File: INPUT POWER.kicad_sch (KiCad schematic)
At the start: 1 part, among them J1 TYPE-C-31-M12_13

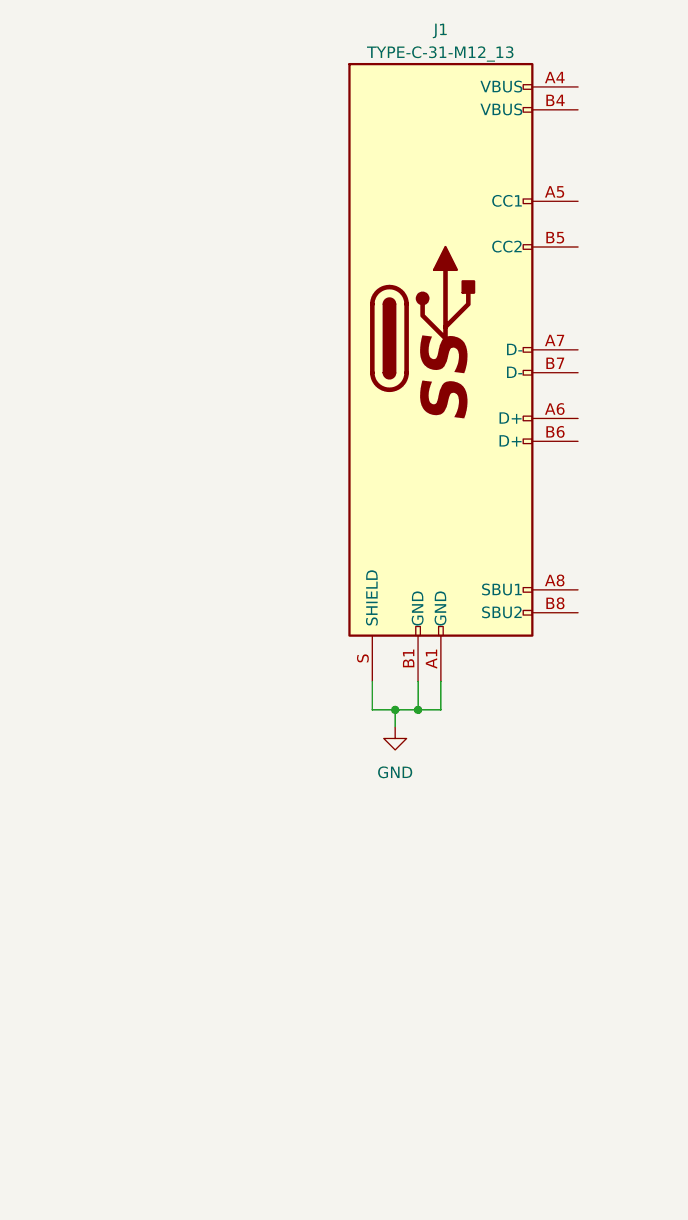
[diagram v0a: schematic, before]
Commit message: completed USB-C wiring and added flash
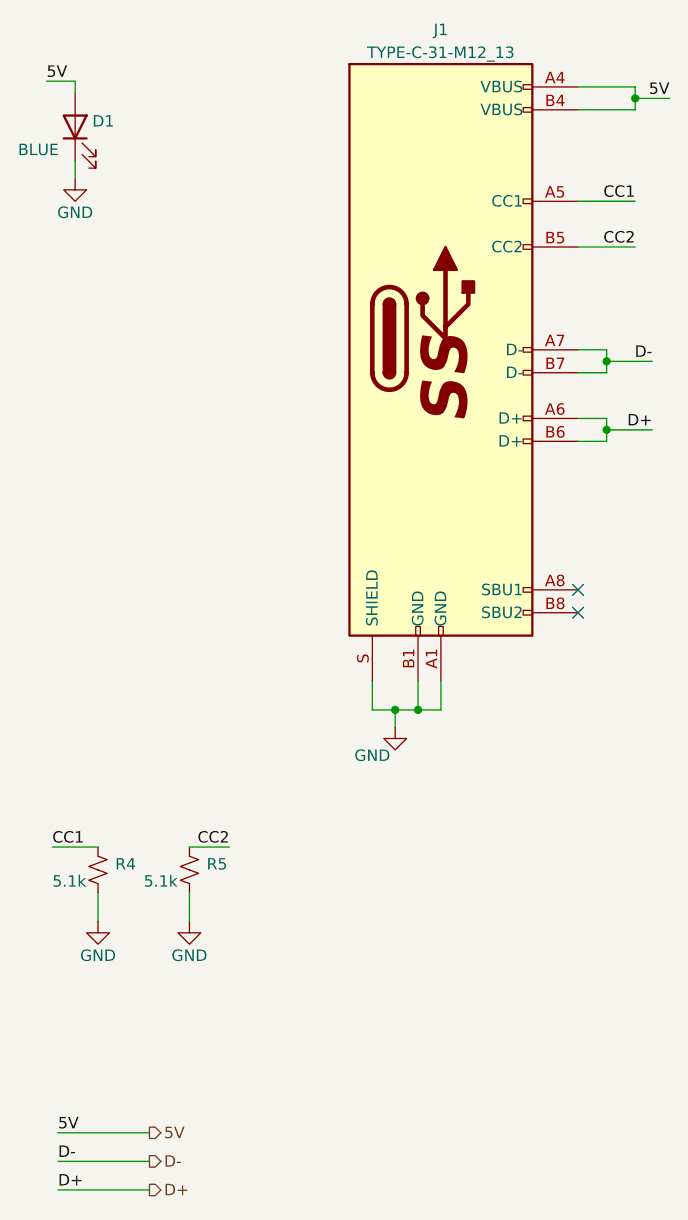
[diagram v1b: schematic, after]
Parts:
- added D1: BLUE, symbol ESP32-S3_DB:LED
- added R4, R5: 5.1k, symbol ESP32-S3_DB:R_Small_US
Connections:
- net GND: now also D1.1 (K), R4.2, R5.2
- net 5V: now reaches J1.A4 (VBUS)
- net 5V: now also J1.B4 (VBUS), D1.2 (A)
- net CC1: now reaches J1.A5 (CC1)
- net CC1: now also R4.1
- net D+: now reaches J1.A6 (D+)
- net D+: now also J1.B6 (D+)
- net D-: now reaches J1.A7 (D-)
- net D-: now also J1.B7 (D-)
- net CC2: now reaches J1.B5 (CC2)
- net CC2: now also R5.1
- no-connect marks 0 -> 2

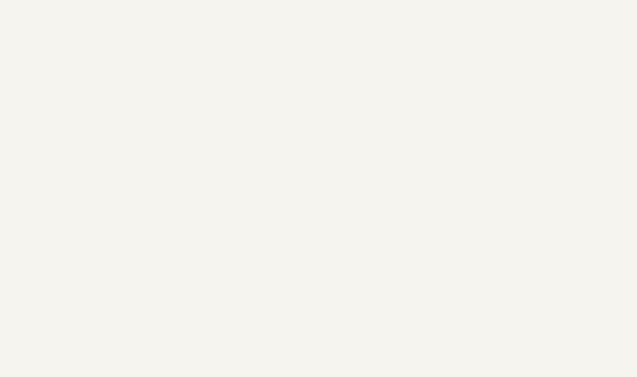
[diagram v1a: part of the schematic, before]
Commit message: Added USB-To-UART Converter
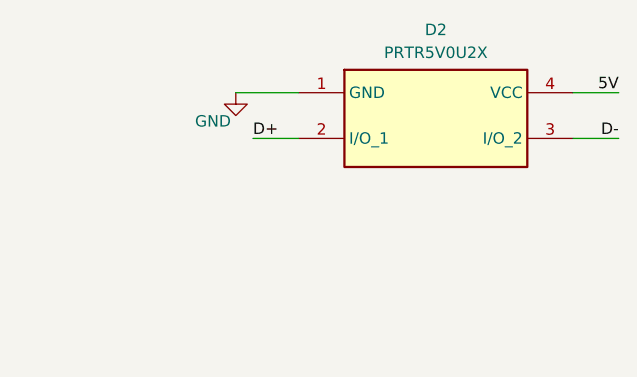
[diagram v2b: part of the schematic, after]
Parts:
- added D2: PRTR5V0U2X, PRTR5V0U2X, symbol ESP32-S3_DB:PRTR5V0U2X
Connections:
- net 5V: now also D2.4 (VCC)
- net D+: now also D2.2 (I/O_1)
- net D-: now also D2.3 (I/O_2)
- net GND: now also D2.1 (GND)
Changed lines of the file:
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@@
+    (stroke (width 0) (type default))
+  )
+  (wire (pts (xy 181.61 36.195) (xy 186.69 36.195))
     (stroke (width 0) (type default))
   )
@@
     (stroke (width 0) (type default))
   )
+  (wire (pts (xy 186.69 31.115) (xy 181.61 31.115))
+    (stroke (width 0) (type default))
+  )
   (wire (pts (xy 66.675 132.08) (xy 66.675 135.255))
     (stroke (width 0) (type default))
@@
     (stroke (width 0) (type default))
   )
+  (wire (pts (xy 146.05 36.195) (xy 151.13 36.195))
+    (stroke (width 0) (type default))
+  )
   (wire (pts (xy 85.09 105.41) (xy 81.915 105.41))
     (stroke (width 0) (type default))
@@
     (stroke (width 0) (type default))
   )
+  (wire (pts (xy 144.145 31.115) (xy 151.13 31.115))
+    (stroke (width 0) (type default))
+  )
   (wire (pts (xy 59.055 135.255) (xy 61.595 135.255))
     (stroke (width 0) (type default))
@@
     (stroke (width 0) (type default))
   )
+  (label "D-" (at 186.69 36.195 180) (fields_autoplaced)
+    (effects (font (size 1.27 1.27)) (justify right bottom))
+  )
   (label "CC2" (at 43.18 150.495 180) (fields_autoplaced)
     (effects (font (size 1.27 1.27)) (justify right bottom))
   )
+  (label "D+" (at 146.05 36.195 0) (fields_autoplaced)
+    (effects (font (size 1.27 1.27)) (justify left bottom))
+  )
   (label "D+" (at 24.13 188.595 0) (fields_autoplaced)
     (effects (font (size 1.27 1.27)) (justify left bottom))
+  )
+  (label "5V" (at 186.69 31.115 180) (fields_autoplaced)
+    (effects (font (size 1.27 1.27)) (justify right bottom))
   )
   (label "D-" (at 90.17 96.52 180) (fields_autoplaced)
@@
   (hierarchical_label "D-" (shape output) (at 34.29 185.42 0) (fields_autoplaced)
     (effects (font (size 1.27 1.27)) (justify left))
+  )
+  (symbol (lib_id "ESP32-S3_DB:PRTR5V0U2X") (at 151.13 31.115 0) (unit 1)
+    (in_bom yes) (on_board yes) (dnp no) (fields_autoplaced)
+    (property "Reference" "D2" (at 166.37 24.13 0)
+      (effects (font (size 1.27 1.27)))
+    )
+    (property "Value" "PRTR5V0U2X" (at 166.37 26.67 0)
+      (effects (font (size 1.27 1.27)))
+    )
+    (property "Footprint" "PRTR5V0U2X" (at 177.8 126.035 0)
+      (effects (font (size 1.27 1.27)) (justify left top) hide)
+    )
+    (property "Datasheet" "https://assets.nexperia.com/documents/data-sheet/PRTR5V0U2X.pdf" (at 177.8 226.035 0)
+      (effects (font (size 1.27 1.27)) (justify left top) hide)
+    )
+    (property "Height" "1.1" (at 177.8 426.035 0)
+      (effects (font (size 1.27 1.27)) (justify left top) hide)
+    )
+    (property "Manufacturer_Name" "Nexperia" (at 177.8 526.035 0)
+      (effects (font (size 1.27 1.27)) (justify left top) hide)
+    )
+    (property "Manufacturer_Part_Number" "PRTR5V0U2X" (at 177.8 626.035 0)
+      (effects (font (size 1.27 1.27)) (justify left top) hide)
+    )
+    (property "Mouser Part Number" "N/A" (at 177.8 726.035 0)
+      (effects (font (size 1.27 1.27)) (justify left top) hide)
+    )
+    (property "Mouser Price/Stock" "https://www.mouser.co.uk/ProductDetail/Nexperia/PRTR5V0U2X?qs=vHuUswq2%252BsxqVTVM0kNyWw%3D%3D" (at 177.8 826.035 0)
+      (effects (font (size 1.27 1.27)) (justify left top) hide)
+    )
+    (property "Arrow Part Number" "" (at 177.8 926.035 0)
+      (effects (font (size 1.27 1.27)) (justify left top) hide)
+    )
+    (property "Arrow Price/Stock" "" (at 177.8 1026.035 0)
+      (effects (font (size 1.27 1.27)) (justify left top) hide)
+    )
+    (pin "1")
+    (pin "2")
+    (pin "3")
+    (pin "4")
+    (instances
+      (project "ESP32-S3_DB"
+        (path "/b7fc4bd3-c219-4455-832b-8d795385dcf1/95090a63-7b3c-4ea0-92b8-aeafe05264cd"
+          (reference "D2") (unit 1)
+        )
+      )
+    )
   )
   (symbol (lib_id "ESP32-S3_DB:GND") (at 61.595 137.16 0) (unit 1)
@@
         )
       )
+    )
+  )
+  (symbol (lib_id "ESP32-S3_DB:GND") (at 144.145 31.115 0) (unit 1)
+    (in_bom yes) (on_board yes) (dnp no)
+    (property "Reference" "#PWR027" (at 144.145 37.465 0)
+      (effects (font (size 1.27 1.27)) hide)
+    )
+    (property "Value" "GND" (at 141.605 34.29 0)
+      (effects (font (size 1.27 1.27)))
+    )
+    (property "Footprint" "" (at 144.145 31.115 0)
+      (effects (font (size 1.27 1.27)) hide)
+    )
+    (property "Datasheet" "" (at 144.145 31.115 0)
+      (effects (font (size 1.27 1.27)) hide)
+    )
+    (pin "1")
+    (instances
+      (project "ESP32-S3_DB"
+        (path "/b7fc4bd3-c219-4455-832b-8d795385dcf1/95090a63-7b3c-4ea0-92b8-aeafe05264cd"
+          (reference "#PWR027") (unit 1)
+        )
+      )

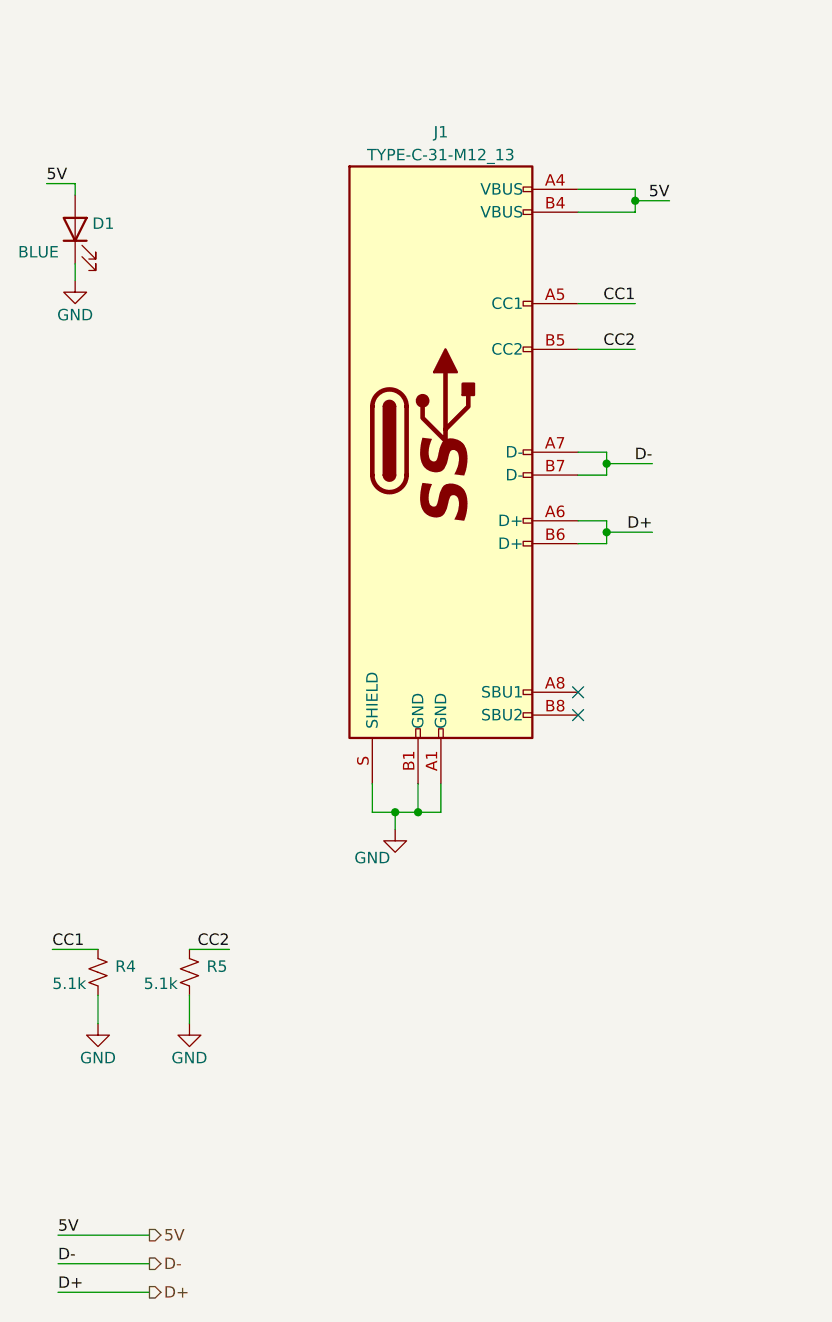
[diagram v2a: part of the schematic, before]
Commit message: Added RS-485 Transceiver
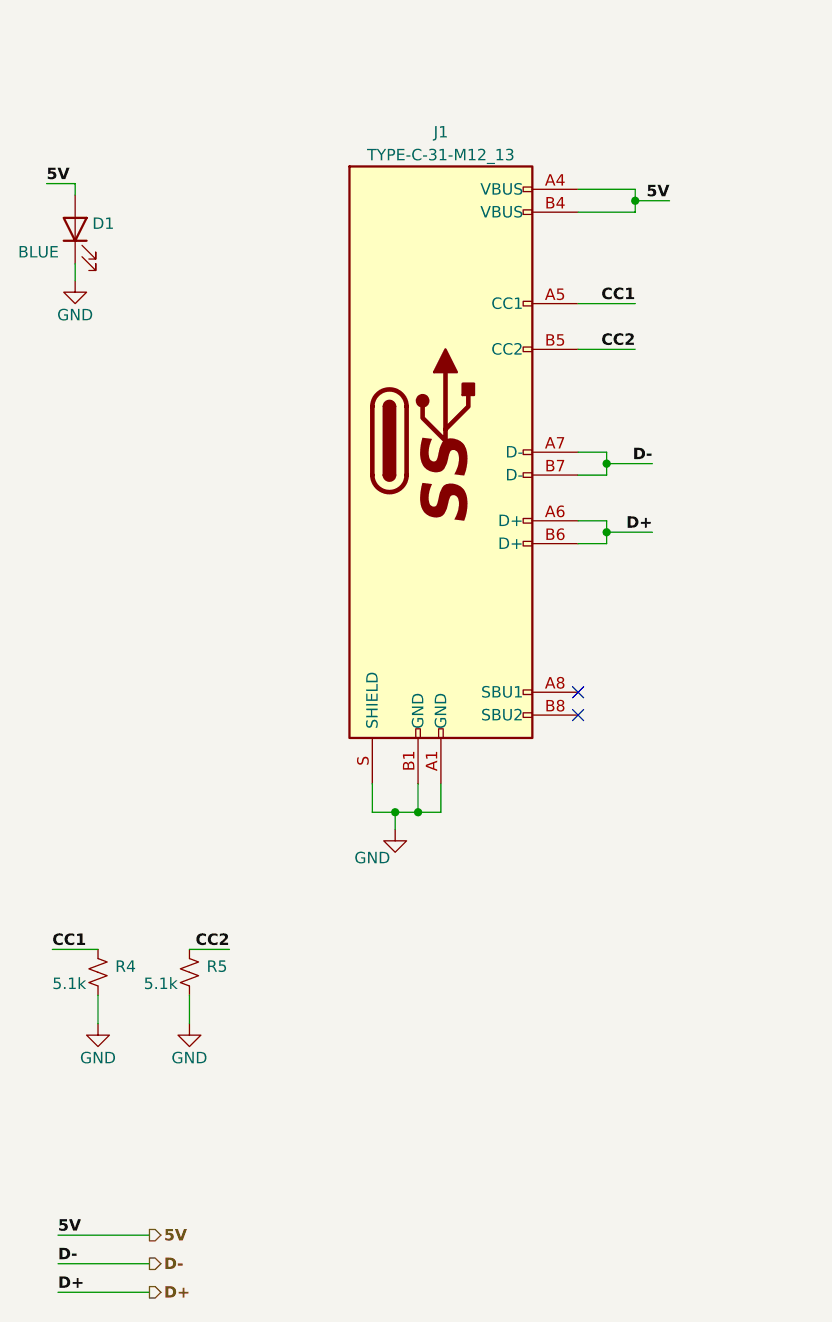
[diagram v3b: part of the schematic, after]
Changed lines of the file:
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@@
     (effects (font (size 1.27 1.27)) (justify right bottom))
   )
-  (label "CC2" (at 43.18 150.495 180) (fields_autoplaced)
-    (effects (font (size 1.27 1.27)) (justify right bottom))
+  (label "5V" (at 22.86 65.405 0) (fields_autoplaced)
+    (effects (font (size 1.27 1.27) (thickness 0.254) bold (color 255 0 0 1)) (justify left bottom))
   )
   (label "D+" (at 146.05 36.195 0) (fields_autoplaced)
@@
   )
   (label "D+" (at 24.13 188.595 0) (fields_autoplaced)
-    (effects (font (size 1.27 1.27)) (justify left bottom))
+    (effects (font (size 1.27 1.27) (thickness 0.254) bold (color 0 0 255 1)) (justify left bottom))
+  )
+  (label "CC1" (at 23.495 150.495 0) (fields_autoplaced)
+    (effects (font (size 1.27 1.27) (thickness 0.254) bold (color 255 153 0 1)) (justify left bottom))
   )
   (label "5V" (at 186.69 31.115 180) (fields_autoplaced)
@@
   )
   (label "D-" (at 90.17 96.52 180) (fields_autoplaced)
-    (effects (font (size 1.27 1.27)) (justify right bottom))
+    (effects (font (size 1.27 1.27) (thickness 0.254) bold (color 0 0 255 1)) (justify right bottom))
   )
   (label "5V" (at 24.13 182.245 0) (fields_autoplaced)
-    (effects (font (size 1.27 1.27)) (justify left bottom))
+    (effects (font (size 1.27 1.27) (thickness 0.254) bold (color 255 0 0 1)) (justify left bottom))
   )
   (label "CC1" (at 88.265 78.74 180) (fields_autoplaced)
-    (effects (font (size 1.27 1.27)) (justify right bottom))
+    (effects (font (size 1.27 1.27) (thickness 0.254) bold (color 255 153 0 1)) (justify right bottom))
   )
   (label "CC2" (at 88.265 83.82 180) (fields_autoplaced)
-    (effects (font (size 1.27 1.27)) (justify right bottom))
+    (effects (font (size 1.27 1.27) (thickness 0.254) bold (color 255 153 0 1)) (justify right bottom))
   )
   (label "5V" (at 92.075 67.31 180) (fields_autoplaced)
-    (effects (font (size 1.27 1.27)) (justify right bottom))
+    (effects (font (size 1.27 1.27) (thickness 0.254) bold (color 255 0 0 1)) (justify right bottom))
   )
   (label "D-" (at 24.13 185.42 0) (fields_autoplaced)
-    (effects (font (size 1.27 1.27)) (justify left bottom))
-  )
-  (label "CC1" (at 23.495 150.495 0) (fields_autoplaced)
-    (effects (font (size 1.27 1.27)) (justify left bottom))
-  )
-  (label "5V" (at 22.86 65.405 0) (fields_autoplaced)
-    (effects (font (size 1.27 1.27)) (justify left bottom))
+    (effects (font (size 1.27 1.27) (thickness 0.254) bold (color 0 0 255 1)) (justify left bottom))
   )
   (label "D+" (at 90.17 104.14 180) (fields_autoplaced)
-    (effects (font (size 1.27 1.27)) (justify right bottom))
+    (effects (font (size 1.27 1.27) (thickness 0.254) bold (color 0 0 255 1)) (justify right bottom))
+  )
+  (label "CC2" (at 43.18 150.495 180) (fields_autoplaced)
+    (effects (font (size 1.27 1.27) (thickness 0.254) bold (color 255 153 0 1)) (justify right bottom))
   )
   (hierarchical_label "D+" (shape output) (at 34.29 188.595 0) (fields_autoplaced)
-    (effects (font (size 1.27 1.27)) (justify left))
+    (effects (font (size 1.27 1.27) (thickness 0.254) bold (color 0 0 255 1)) (justify left))
   )
   (hierarchical_label "5V" (shape output) (at 34.29 182.245 0) (fields_autoplaced)
-    (effects (font (size 1.27 1.27)) (justify left))
+    (effects (font (size 1.27 1.27) (thickness 0.254) bold (color 255 0 0 1)) (justify left))
   )
   (hierarchical_label "D-" (shape output) (at 34.29 185.42 0) (fields_autoplaced)
-    (effects (font (size 1.27 1.27)) (justify left))
+    (effects (font (size 1.27 1.27) (thickness 0.254) bold (color 0 0 255 1)) (justify left))
   )
   (symbol (lib_id "ESP32-S3_DB:PRTR5V0U2X") (at 151.13 31.115 0) (unit 1)
